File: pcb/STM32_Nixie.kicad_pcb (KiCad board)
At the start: 4 copper layers, 185 parts, among them J1 CON_SAMTEC_14P_2R_1m27_P_KEY_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, J2 CONN_USBC_RCPT_USB2.0_USB4085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, Q1 NFET_250V_10A_TPH1110FNH,L1Q, Q2 NFET_60V_0A5_2N7002KT1G, SW1 ENC_SPST_24PPR_PEC12R-4225F-S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, U1 IC_SR_MC_HV5622PG-G, U2 IC_SR_MC_HV5622PG-G, U3 IC_MCU_STM32F100C4T6B_48LQFP, U4 IC_LVL_ONSEMI_MC14504BDTR2G, U5 REG_SW_BOOST_TI_TLV61046ADBV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

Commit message: Placement wip
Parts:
- N1, N2: value IN-3 -> Val**
- N3, N4, N5, N6, N7, N8: value IN-14 -> Val**
- moved J1 34.8 mm to (82.6, 104.7)
- moved TP1 32.4 mm to (134.8, 128.8)
- moved R14 23.7 mm to (174.0, 87.0), turned to -90 degrees
- moved R13 21.6 mm to (152.0, 87.0)
- moved S1 20.3 mm to (108.5, 131.8)
- moved S2 20.3 mm to (115.4, 131.8)
- moved R4 10.5 mm to (130.1, 87.0)
- moved FB1 9.65 mm to (128.2, 105.7), turned to -90 degrees
- moved R36 9.29 mm to (134.0, 108.9)
- moved R6 9.26 mm to (125.1, 111.5)
- moved R39 9.21 mm to (134.0, 107.4)
- moved R35 9.20 mm to (134.0, 112.9)
- moved R38 9.14 mm to (134.0, 111.4)
- moved C49 8.96 mm to (131.8, 108.2)
- moved C48 8.86 mm to (131.8, 112.2)
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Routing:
- net /Power/GATE_R: track 5.32 -> 19.7 mm
- net /Power/CS_RAW: track 3.51 -> 12.6 mm, vias 1 -> 2
- net +12V: track 0.00 -> 3.54 mm
- net /Power/CS_FILT: track 0.00 -> 2.97 mm
- net GND: track 9.20 -> 6.71 mm, vias 14 -> 12
- net /Power/CS_FILT_R: track 0.00 -> 2.11 mm

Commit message: Routing progress! Maybe 30% done.
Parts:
- added REF**: MountingHole_3.2mm_M3_Pad_Via, MountingHole:MountingHole_3.2mm_M3_Pad_Via, F.Cu at (224.3, 66.2)
- added REF**: MountingHole_3.2mm_M3_Pad_Via, MountingHole:MountingHole_3.2mm_M3_Pad_Via, F.Cu at (79.7, 66.2)
- added REF**: MountingHole_3.2mm_M3_Pad_Via, MountingHole:MountingHole_3.2mm_M3_Pad_Via, F.Cu at (224.3, 113.8)
- added REF**: MountingHole_3.2mm_M3_Pad_Via, MountingHole:MountingHole_3.2mm_M3_Pad_Via, F.Cu at (79.7, 113.8)
- JP1: moved to B.Cu
- N1, N2: value Val** -> IN-3
- N3, N4, N5, N6, N7, N8: value Val** -> IN-14
- S1, S2: value SW_TACT_PTS645SM43SMTR92_LFS -> SW_TACT_KMR211NG LFS; footprint arjun_footprints:Switch_Tactile_SMD_6x6mm_PTS645 -> arjun_footprints:SW_Push_1P1T_NO_CK_KMR2
- moved S2 43.3 mm to (80.8, 105.7), turned to 0 degrees
- moved S1 41.9 mm to (80.8, 100.4), turned to 180 degrees
- moved J1 33.6 mm to (115.4, 111.9), turned to -90 degrees
- moved TP6 31.2 mm to (193.0, 108.5)
- moved TP1 30.9 mm to (114.8, 105.2), turned to 0 degrees
- moved R61 29.5 mm to (112.6, 98.3), turned to 90 degrees
- moved R62 28.4 mm to (110.9, 98.3), turned to 90 degrees
- moved R63 27.5 mm to (109.2, 98.3), turned to 90 degrees
- moved R60 13.9 mm to (141.0, 101.7), turned to 180 degrees
- moved R58 11.2 mm to (141.0, 98.3), turned to 180 degrees
- moved R59 9.95 mm to (141.0, 100.0), turned to 180 degrees
- moved R69 5.53 mm to (142.7, 115.2)
- moved D10 5.53 mm to (140.9, 115.2)
- moved C37 3.78 mm to (156.9, 115.2)
- moved C38 3.78 mm to (155.0, 115.2)
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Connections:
- net /MCU/UART_BL_RX renamed /MCU/UART1_BL_RX
- net /MCU/UART_BL_TX renamed /MCU/UART1_BL_TX
- net /MCU/UART_VCP_RX renamed /MCU/UART2_VCP_RX
- net /MCU/UART_VCP_TX renamed /MCU/UART2_VCP_TX
- U4 pad 2: /SPI_SCK_12V -> /SPI_PICO_12V
- U4 pad 3: /SPI_SCK_3V3 -> /SPI_PICO_3V3
- U4 pad 4: /SPI_PICO_12V -> /SPI_SCK_12V
- U4 pad 5: /SPI_PICO_3V3 -> /SPI_SCK_3V3
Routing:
- net GND: track 6.71 -> 82.4 mm, vias 12 -> 48
- net /MCU/UART1_BL_RX: track 0.00 -> 50.3 mm, vias 0 -> 2
- net +3.3V: track 0.00 -> 46.7 mm, vias 0 -> 19
- net /PWM_nBL_3V3: track 0.00 -> 44.4 mm, vias 0 -> 2
- net /MCU/UART1_BL_TX: track 0.00 -> 44.1 mm, vias 0 -> 2
- net /SPI_nCS_nLE_3V3: track 0.00 -> 41.5 mm
- net /nPOL_3V3: track 0.00 -> 39.1 mm, vias 0 -> 2
- net /SPI_SCK_3V3: track 0.00 -> 38.6 mm
- net /SPI_PICO_3V3: track 0.00 -> 36.0 mm
- net /MCU/UART2_VCP_RX: track 0.00 -> 31.6 mm, vias 0 -> 2
- net /MCU/UART2_VCP_TX: track 0.00 -> 28.0 mm, vias 0 -> 2
- net /MCU/nRST: track 0.00 -> 27.1 mm, vias 0 -> 3
- net /MCU/SWCLK: track 0.00 -> 22.0 mm, vias 0 -> 2
- net /MCU/SWO: track 0.00 -> 21.7 mm, vias 0 -> 2
- net /MCU/SWDIO: track 0.00 -> 21.4 mm, vias 0 -> 2
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- added copper zone on F.Cu, net +3.3V
- added copper zone on F.Cu, net /Power/VIN_3V3
- added copper zone on F.Cu, net GNDPWR
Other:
- board outline added: 154 x 57 mm

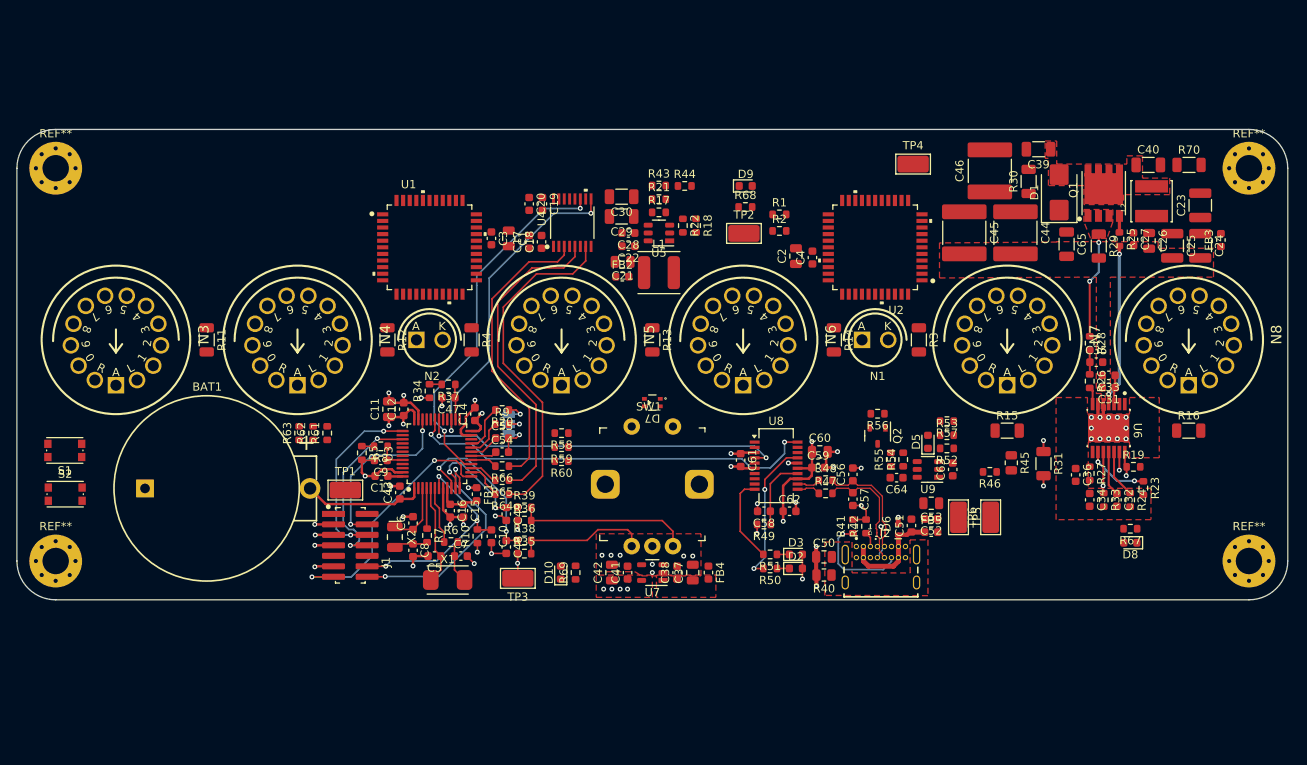
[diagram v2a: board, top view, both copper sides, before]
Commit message: 50% done routing. Power pour progress!
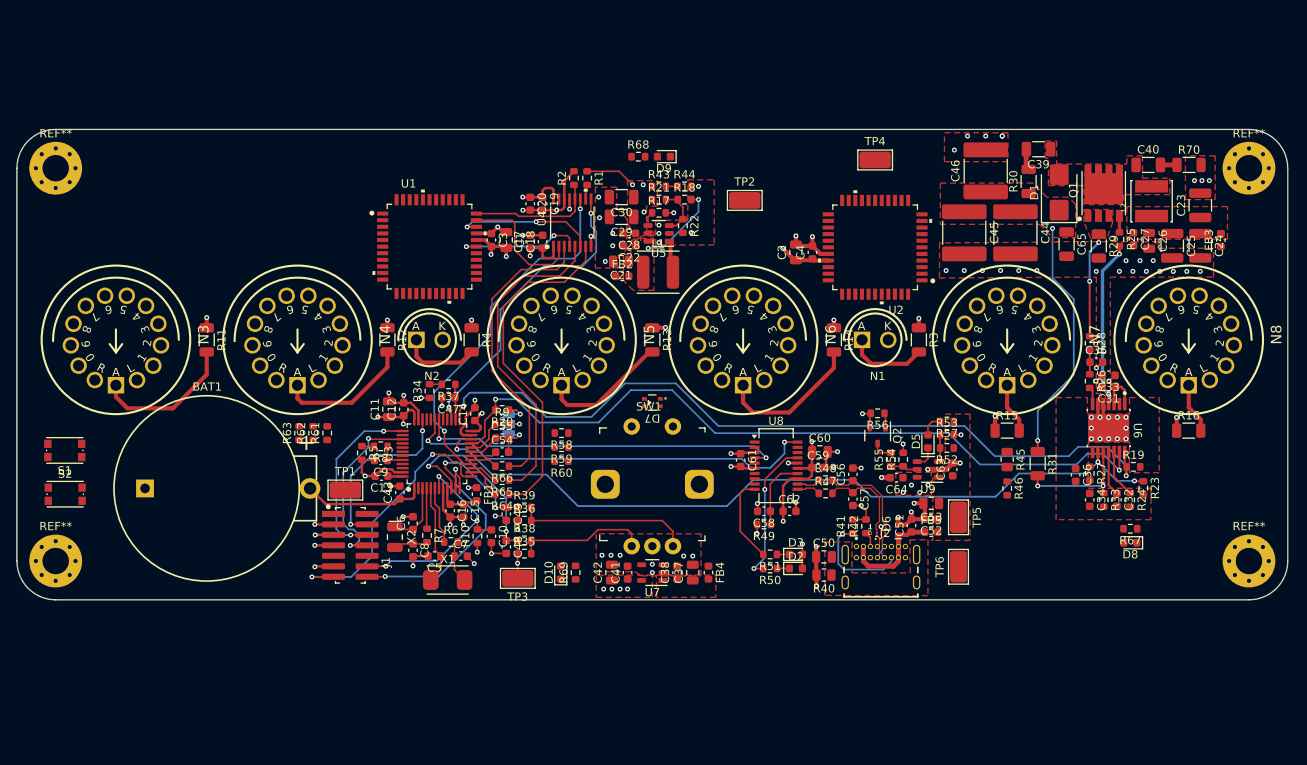
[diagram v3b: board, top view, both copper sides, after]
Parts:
- moved R2 25.7 mm to (142.5, 67.4), turned to 90 degrees
- moved R1 23.7 mm to (144.1, 67.4), turned to -90 degrees
- moved R68 14.3 mm to (150.3, 64.8)
- moved D9 10.5 mm to (153.4, 64.8), turned to 180 degrees
- moved TP6 7.16 mm to (189.1, 114.5)
- moved TP4 4.63 mm to (179.0, 65.2)
- moved TP2 4.00 mm to (163.2, 70.1)
- moved R18 3.45 mm to (155.9, 70.0), turned to 0 degrees
- moved R46 2.90 mm to (195.0, 105.0), turned to -90 degrees
- moved R31 0.70 mm to (198.7, 102.0)
- moved R45 0.64 mm to (195.0, 101.5)
- moved C4 0.62 mm to (171.4, 76.4)
- moved C46 0.50 mm to (192.4, 66.5)
- moved C2 0.45 mm to (169.4, 76.4)
- moved C1 0.36 mm to (134.3, 74.9)
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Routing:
- net +12V: track 3.54 -> 117.1 mm, vias 0 -> 7
- net /MCU/EN_180V: track 3.03 -> 95.5 mm, vias 1 -> 2
- net /MCU/DITHOFF_180V: track 7.67 -> 94.8 mm, vias 2 -> 3
- net /MCU/PG_180V: track 7.92 -> 92.7 mm, vias 1 -> 2
- net GND: track 82.4 -> 131.7 mm, vias 48 -> 103
- net 180V: track 1.54 -> 40.3 mm, vias 1 -> 10
- net /Nixie Display/M2/NIXIE_A: track 0.00 -> 17.1 mm
- net /SPI_nCS_nLE_12V: track 0.00 -> 17.1 mm, vias 0 -> 2
- net /Nixie Display/H1/NIXIE_A: track 0.00 -> 16.7 mm
- net /SPI_PICO_12V: track 0.00 -> 15.9 mm
- net /PWM_nBL_12V: track 0.00 -> 15.7 mm
- net /Nixie Display/H2/NIXIE_A: track 0.00 -> 15.6 mm
- net /SPI_SCK_12V: track 0.00 -> 15.4 mm, vias 0 -> 2
- net /Nixie Display/M1/NIXIE_A: track 0.00 -> 15.0 mm
- net /Power/VIN_12V: track 0.00 -> 10.3 mm, vias 0 -> 2
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- added copper zone on F.Cu, net +12V
- added copper zone on In2.Cu, net +12V
- added copper zone on F.Cu, net +5V
- added copper zone on In2.Cu, net +5V
- added copper zone on F.Cu, net /Power/VIN_12V
- added copper zone on F.Cu, net /Power/VIN_180V
- added copper zone on F.Cu, net /USB Connector/USB_VBUS
- added copper zone on F.Cu, net 180V
- added copper zone on In2.Cu, net 180V
- added copper zone on In1.Cu, net GND
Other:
- board text added: "- Controlled impedance stackup from JLC has 0.1mm pregrep between L1-L2 and L3-L4. - The regular stackup is 0.2mm between L1-L2 and L3-L4. This should be more than sufficient to isolate 180VDC between layers."

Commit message: Making progress on nixie tube signal routing
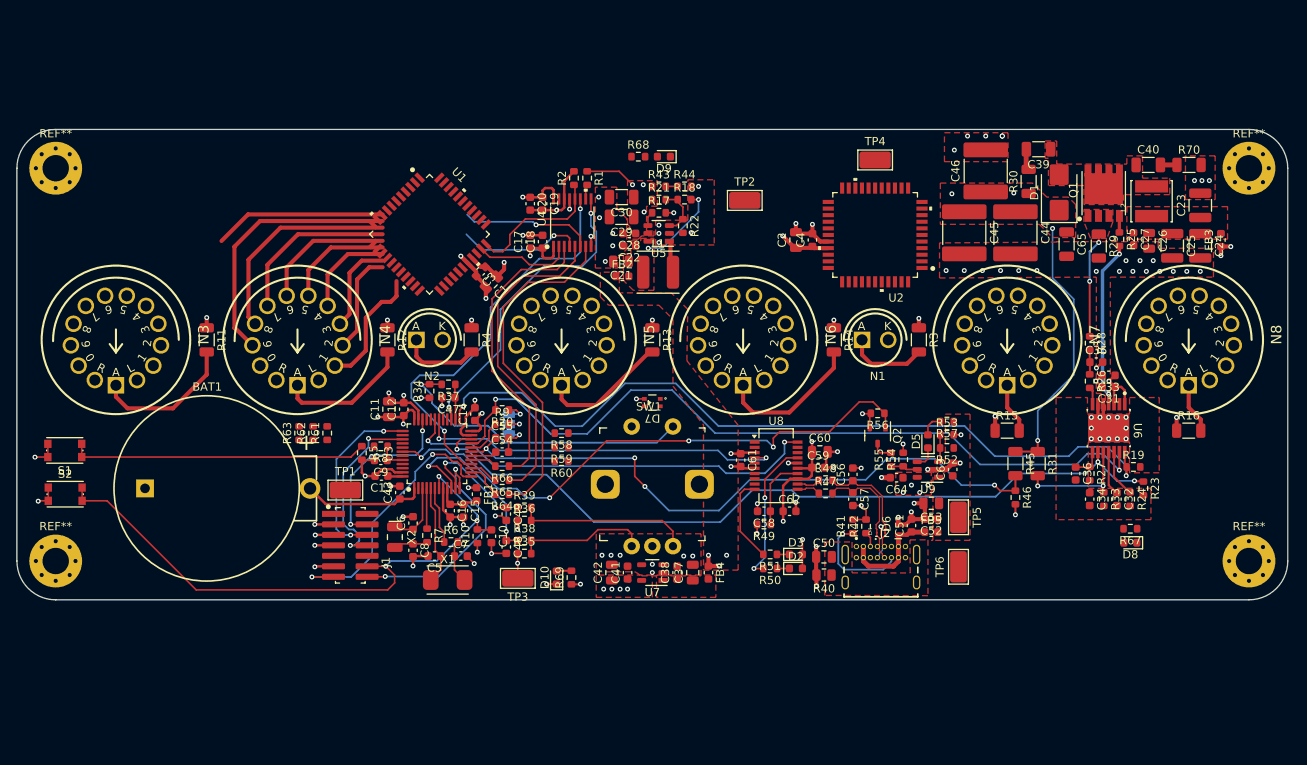
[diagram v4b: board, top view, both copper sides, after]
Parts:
- R45: footprint Resistor_SMD:R_0805_2012Metric -> Resistor_SMD:R_1206_3216Metric
- moved C1 5.41 mm to (132.5, 80.0), turned to -135 degrees
- moved C3 4.02 mm to (131.2, 78.7), turned to -135 degrees
- moved C2 1.50 mm to (169.4, 74.9)
- moved C4 1.50 mm to (171.4, 74.9)
- moved U1 1.50 mm to (125.0, 74.2), turned to -45 degrees
- moved U2 1.50 mm to (179.0, 74.3)
- moved R46 1.49 mm to (196.0, 106.1)
- moved R45 1.12 mm to (196.0, 102.0)
- moved D10 0.78 mm to (140.4, 115.8)
- moved R69 0.78 mm to (142.2, 115.8)
- moved C36 0.16 mm to (203.3, 103.2)
- moved C32 0.09 mm to (208.3, 106.3)
- moved C34 0.09 mm to (205.0, 106.3)
- moved R24 0.09 mm to (209.9, 106.3)
- moved R33 0.09 mm to (206.7, 106.3)
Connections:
- U1 pad 1: /Nixie Display/M1_1 -> /Nixie Display/M1_2
- U1 pad 10: /Nixie Display/H2_2 -> /Nixie Display/H2_3
- U1 pad 11: /Nixie Display/H2_1 -> /Nixie Display/H2_2
- U1 pad 12: /Nixie Display/H2_0 -> /Nixie Display/H2_1
- U1 pad 13: /Nixie Display/H1_9 -> /Nixie Display/H1_0
- U1 pad 14: /Nixie Display/H1_8 -> /Nixie Display/H1_9
- U1 pad 15: /Nixie Display/H1_7 -> /Nixie Display/H1_8
- U1 pad 16: /Nixie Display/H1_6 -> /Nixie Display/H1_7
- U1 pad 17: /Nixie Display/H1_5 -> /Nixie Display/H1_6
- U1 pad 18: /Nixie Display/H1_4 -> /Nixie Display/H1_5
- U1 pad 19: /Nixie Display/H1_3 -> /Nixie Display/H1_4
- U1 pad 2: /Nixie Display/M1_0 -> /Nixie Display/M1_1
- U1 pad 20: /Nixie Display/H1_2 -> /Nixie Display/H1_3
- U1 pad 21: /Nixie Display/H1_1 -> /Nixie Display/H1_2
- U1 pad 22: /Nixie Display/H1_0 -> /Nixie Display/H1_1
- U1 pad 3: /Nixie Display/H2_9 -> /Nixie Display/H2_0
- U1 pad 35: /Nixie Display/M2_1 -> /Nixie Display/M2_2
- U1 pad 36: /Nixie Display/M2_0 -> /Nixie Display/M2_1
- U1 pad 37: /Nixie Display/M1_9 -> /Nixie Display/M1_0
- U1 pad 38: /Nixie Display/M1_8 -> /Nixie Display/M1_9
- U1 pad 39: /Nixie Display/M1_7 -> /Nixie Display/M1_8
- U1 pad 4: /Nixie Display/H2_8 -> /Nixie Display/H2_9
- U1 pad 40: /Nixie Display/M1_6 -> /Nixie Display/M1_7
- U1 pad 41: /Nixie Display/M1_5 -> /Nixie Display/M1_6
- U1 pad 42: /Nixie Display/M1_4 -> /Nixie Display/M1_5
- U1 pad 43: /Nixie Display/M1_3 -> /Nixie Display/M1_4
- U1 pad 44: /Nixie Display/M1_2 -> /Nixie Display/M1_3
- U1 pad 5: /Nixie Display/H2_7 -> /Nixie Display/H2_8
- U1 pad 6: /Nixie Display/H2_6 -> /Nixie Display/H2_7
- U1 pad 7: /Nixie Display/H2_5 -> /Nixie Display/H2_6
- U1 pad 8: /Nixie Display/H2_4 -> /Nixie Display/H2_5
- U1 pad 9: /Nixie Display/H2_3 -> /Nixie Display/H2_4
- U2 pad 1: /Nixie Display/S2_3 -> /Nixie Display/S2_4
- U2 pad 10: /Nixie Display/S1_4 -> /Nixie Display/S1_5
- U2 pad 11: /Nixie Display/S1_3 -> /Nixie Display/S1_4
- U2 pad 12: /Nixie Display/S1_2 -> /Nixie Display/S1_3
- U2 pad 13: /Nixie Display/S1_1 -> /Nixie Display/S1_2
- U2 pad 14: /Nixie Display/S1_0 -> /Nixie Display/S1_1
- U2 pad 15: /Nixie Display/M2_9 -> /Nixie Display/M2_0
- U2 pad 16: /Nixie Display/M2_8 -> /Nixie Display/M2_9
- U2 pad 17: /Nixie Display/M2_7 -> /Nixie Display/M2_8
- U2 pad 18: /Nixie Display/M2_6 -> /Nixie Display/M2_7
- U2 pad 19: /Nixie Display/M2_5 -> /Nixie Display/M2_6
- U2 pad 2: /Nixie Display/S2_2 -> /Nixie Display/S2_3
- U2 pad 20: /Nixie Display/M2_4 -> /Nixie Display/M2_5
- U2 pad 21: /Nixie Display/M2_3 -> /Nixie Display/M2_4
- U2 pad 22: /Nixie Display/M2_2 -> /Nixie Display/M2_3
- U2 pad 3: /Nixie Display/S2_1 -> /Nixie Display/S2_2
- U2 pad 39: /Nixie Display/S2_9 -> /Nixie Display/S2_0
- U2 pad 4: /Nixie Display/S2_0 -> /Nixie Display/S2_1
- U2 pad 40: /Nixie Display/S2_8 -> /Nixie Display/S2_9
- U2 pad 41: /Nixie Display/S2_7 -> /Nixie Display/S2_8
- U2 pad 42: /Nixie Display/S2_6 -> /Nixie Display/S2_7
- U2 pad 43: /Nixie Display/S2_5 -> /Nixie Display/S2_6
- U2 pad 44: /Nixie Display/S2_4 -> /Nixie Display/S2_5
- U2 pad 5: /Nixie Display/S1_9 -> /Nixie Display/S1_0
- U2 pad 6: /Nixie Display/S1_8 -> /Nixie Display/S1_9
- U2 pad 7: /Nixie Display/S1_7 -> /Nixie Display/S1_8
- U2 pad 8: /Nixie Display/S1_6 -> /Nixie Display/S1_7
- U2 pad 9: /Nixie Display/S1_5 -> /Nixie Display/S1_6
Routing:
- net /MCU/SENSE_180V: track 3.69 -> 78.4 mm, vias 0 -> 4
- net /MCU/SET_ILIM: track 1.75 -> 70.0 mm, vias 0 -> 4
- net /MCU/nRST: track 27.1 -> 73.9 mm
- net /User Input/nENC_PB: track 1.49 -> 37.8 mm, vias 0 -> 1
- net /MCU/BOOT0_SW: track 1.49 -> 36.1 mm
- net /Nixie Display/H2_9: track 0.00 -> 32.2 mm
- net /Nixie Display/H2_8: track 0.00 -> 26.0 mm
- net /Nixie Display/H2_0: track 0.00 -> 20.9 mm
- net /Nixie Display/H2_7: track 0.00 -> 20.5 mm
- net /Nixie Display/H2_6: track 0.00 -> 16.4 mm
- net /Nixie Display/H2_1: track 0.00 -> 15.1 mm
- net /Nixie Display/H2_5: track 0.00 -> 13.3 mm
- net /Nixie Display/H2_2: track 0.00 -> 12.4 mm
- net /Nixie Display/H2_4: track 0.00 -> 11.5 mm
- net /Nixie Display/H2_3: track 0.00 -> 11.3 mm
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- added copper zone on In2.Cu, net +3.3V
